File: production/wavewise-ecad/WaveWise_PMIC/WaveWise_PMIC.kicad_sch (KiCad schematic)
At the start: 0 parts

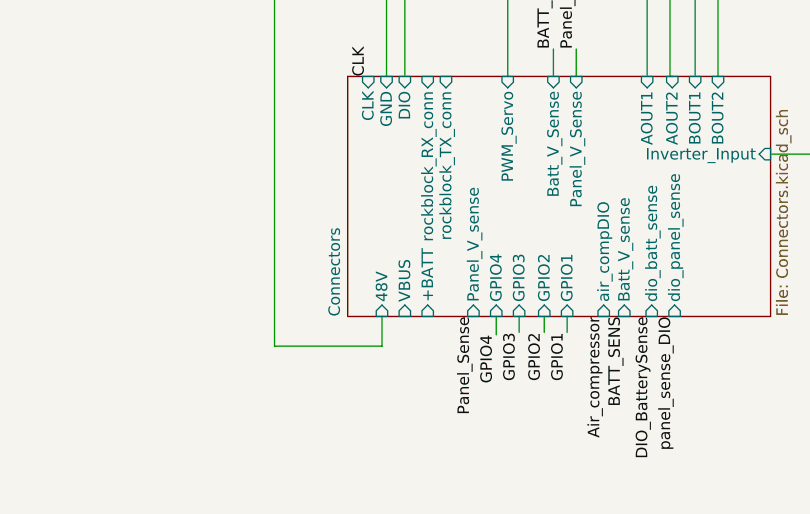
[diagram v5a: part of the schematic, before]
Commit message: added most footprints still need polulu footprint
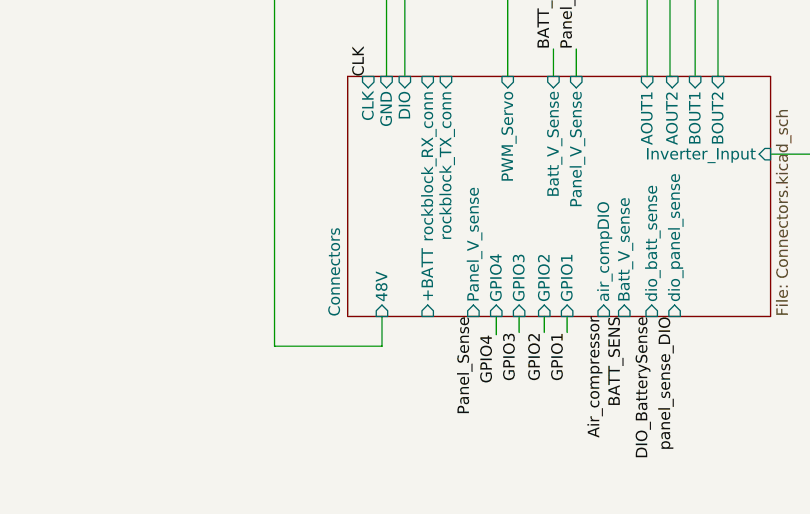
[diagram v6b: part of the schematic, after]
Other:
- sheet Connectors ports: added none; removed VBUS
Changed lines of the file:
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@@
-      (effects (font (size 1.27 1.27)) (justify left))
-    )
-    (pin "VBUS" input (at 109.474 145.034 270)
       (effects (font (size 1.27 1.27)) (justify left))
     )

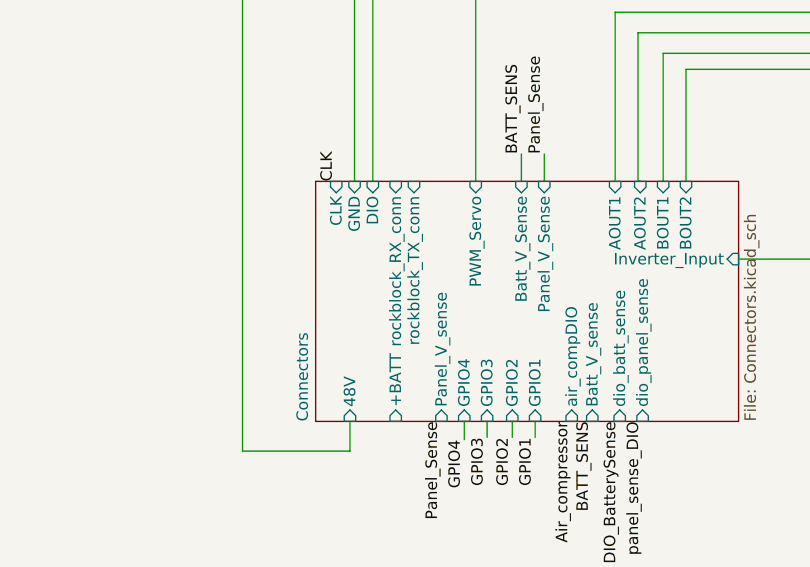
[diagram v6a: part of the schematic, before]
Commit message: More stuff done to PCB Added polulu
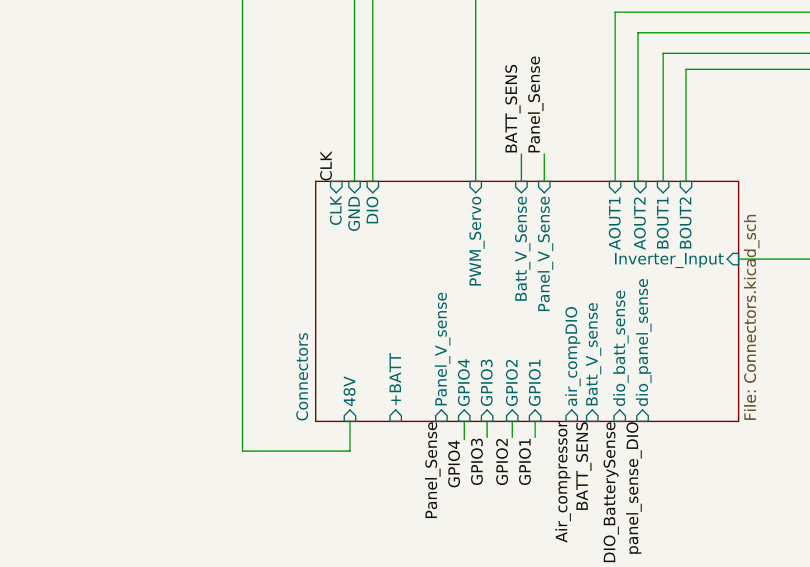
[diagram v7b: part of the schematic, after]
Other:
- sheet Connectors ports: added none; removed rockblock_RX_conn, rockblock_TX_conn
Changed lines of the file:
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@@
       (effects (font (size 1.27 1.27)) (justify left))
-    )
-    (pin "rockblock_RX_conn" input (at 112.014 118.364 90)
-      (effects (font (size 1.27 1.27)) (justify right))
-    )
-    (pin "rockblock_TX_conn" input (at 114.046 118.364 90)
-      (effects (font (size 1.27 1.27)) (justify right))
     )
     (pin "CLK" input (at 105.41 118.364 90)

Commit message: Prelim board layout
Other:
- sheet Connectors ports: added BATT_SENSE_DIO, BICO_UART_RX, BICO_UART_TX, PANEL_SENSE_DIO, SWCLK, SWDIO; removed +BATT, 48V, Batt_V_sense, CLK, DIO, GND, Panel_V_sense, air_compDIO, dio_batt_sense, dio_panel_sense
- sheet PICO (BICO) ports: added BATT_SENSE_DIO, GPIO1, GPIO2, GPIO3, MOTOR_BEMF, MOTOR_DIR/AIN2, MOTOR_SLP, MOTOR_SPI0_CSn, MOTOR_SPI0_RX, MOTOR_SPI0_SCK, MOTOR_SPI0_TX, MOTOR_STALL, MOTOR_STEP/AIN1, PANEL_SENSE_DIO, SWCLK, SWDIO, UART0_Rx, UART0_TX; removed BEMF, B_RX, B_TX, CLK, DIO, GND, GPIO_1, GPIO_2, GPIO_3, MISO1, MOSI1, SCK, SCS, STALL, battsensDIO, panelsensDIO, ~SLP
- sheet Pneumatic Control ports: added DIR/AIN2, SCLK, SDATI, SDATO, STEP/AIN1; removed CLK, MISO1, MOSI1
- sheet Power ports: added none; removed 48V
